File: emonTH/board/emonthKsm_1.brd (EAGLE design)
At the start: 50 x 50 mm, 9 parts

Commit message: Added board
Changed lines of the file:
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@@
 </variantdefs>
 <classes>
-<class number="0" name="default" width="0" drill="0">
+<class number="0" name="default" width="0.3" drill="0.5">
+<clearance class="0" value="0.3"/>
 </class>
 </classes>
-<designrules name="default">
+<designrules name="SeeedStudio_2layer_DRU_no_angle_20140221">
 <description language="de">&lt;b&gt;EAGLE Design Rules&lt;/b&gt;
 &lt;p&gt;
@@
 necessary adjustments and save your customized
 design rules under a new name.</description>
+<description language="zh">&lt;b&gt;Seeed Studio EAGLE Design Rules&lt;/b&gt;
+</description>
 <param name="layerSetup" value="(1*16)"/>
-<param name="mtCopper" value="0.035mm 0.035mm 0.035mm 0.035mm 0.035mm 0.035mm 0.035mm 0.035mm 0.035mm 0.035mm 0.035mm 0.035mm 0.035mm 0.035mm 0.035mm 0.035mm"/>
-<param name="mtIsolate" value="1.5mm 0.15mm 0.2mm 0.15mm 0.2mm 0.15mm 0.2mm 0.15mm 0.2mm 0.15mm 0.2mm 0.15mm 0.2mm 0.15mm 0.2mm"/>
-<param name="mdWireWire" value="8mil"/>
-<param name="mdWirePad" value="8mil"/>
-<param name="mdWireVia" value="8mil"/>
-<param name="mdPadPad" value="8mil"/>
-<param name="mdPadVia" value="8mil"/>
-<param name="mdViaVia" value="8mil"/>
-<param name="mdSmdPad" value="8mil"/>
-<param name="mdSmdVia" value="8mil"/>
-<param name="mdSmdSmd" value="8mil"/>
+<param name="mtCopper" value="0.035mm 0.0175mm 0.035mm 0.035mm 0.035mm 0.035mm 0.035mm 0.035mm 0.035mm 0.035mm 0.035mm 0.035mm 0.035mm 0.035mm 0.0175mm 0.035mm"/>
+<param name="mtIsolate" value="1.5mm 1.1mm 0.2mm 0.15mm 0.2mm 0.15mm 0.2mm 0.15mm 0.2mm 0.15mm 0.2mm 0.15mm 0.2mm 0.15mm 0.2mm"/>
+<param name="mdWireWire" value="6mil"/>
+<param name="mdWirePad" value="6mil"/>
+<param name="mdWireVia" value="6mil"/>
+<param name="mdPadPad" value="6mil"/>
+<param name="mdPadVia" value="6mil"/>
+<param name="mdViaVia" value="6mil"/>
+<param name="mdSmdPad" value="0mil"/>
+<param name="mdSmdVia" value="0mil"/>
+<param name="mdSmdSmd" value="0mil"/>
 <param name="mdViaViaSameLayer" value="8mil"/>
 <param name="mnLayersViaInSmd" value="2"/>
-<param name="mdCopperDimension" value="40mil"/>
-<param name="mdDrill" value="8mil"/>
+<param name="mdCopperDimension" value="10mil"/>
+<param name="mdDrill" value="10mil"/>
 <param name="mdSmdStop" value="0mil"/>
-<param name="msWidth" value="10mil"/>
-<param name="msDrill" value="24mil"/>
-<param name="msMicroVia" value="9.99mm"/>
+<param name="msWidth" value="6mil"/>
+<param name="msDrill" value="12mil"/>
+<param name="msMicroVia" value="12mil"/>
 <param name="msBlindViaRatio" value="0.5"/>
 <param name="rvPadTop" value="0.25"/>
@@
 <param name="rlMinPadBottom" value="10mil"/>
 <param name="rlMaxPadBottom" value="20mil"/>
-<param name="rlMinViaOuter" value="8mil"/>
+<param name="rlMinViaOuter" value="6mil"/>
 <param name="rlMaxViaOuter" value="20mil"/>
-<param name="rlMinViaInner" value="8mil"/>
+<param name="rlMinViaInner" value="6mil"/>
 <param name="rlMaxViaInner" value="20mil"/>
 <param name="rlMinMicroViaOuter" value="4mil"/>
@@
 <param name="psTop" value="-1"/>
 <param name="psBottom" value="-1"/>
-<param name="psFirst" value="-1"/>
+<param name="psFirst" value="0"/>
 <param name="psElongationLong" value="100"/>
 <param name="psElongationOffset" value="100"/>
 <param name="mvStopFrame" value="1"/>
 <param name="mvCreamFrame" value="0"/>
-<param name="mlMinStopFrame" value="4mil"/>
-<param name="mlMaxStopFrame" value="4mil"/>
+<param name="mlMinStopFrame" value="2mil"/>
+<param name="mlMaxStopFrame" value="2mil"/>
 <param name="mlMinCreamFrame" value="0mil"/>
 <param name="mlMaxCreamFrame" value="0mil"/>
-<param name="mlViaStopLimit" value="0mil"/>
+<param name="mlViaStopLimit" value="100mil"/>
 <param name="srRoundness" value="0"/>
 <param name="srMinRoundness" value="0mil"/>
@@
 <param name="checkAngle" value="0"/>
 <param name="checkFont" value="1"/>
-<param name="checkRestrict" value="1"/>
+<param name="checkRestrict" value="0"/>
 <param name="useDiameter" value="13"/>
 <param name="maxErrors" value="50"/>
@@
 <param name="RoutingGrid" value="50mil"/>
 <param name="AutoGrid" value="1"/>
-<param name="Efforts" value="0"/>
+<param name="Efforts" value="2"/>
 <param name="TopRouterVariant" value="1"/>
 <param name="tpViaShape" value="round"/>
@@
 <param name="PrefDir.14" value="0"/>
 <param name="PrefDir.15" value="0"/>
-<param name="PrefDir.16" value="a"/>
+<param name="PrefDir.16" value="0"/>
 <param name="cfVia" value="8"/>
 <param name="cfNonPref" value="5"/>
@@
 <element name="ARDUINO" library="Arduino-clone" package="ABK-PRO-MINI" value="ABK-PRO-MINI" x="11.91" y="33.91"/>
 <element name="RFM69" library="Eagle-JeeLabs" package="RFM12B/69CW" value="RFM12B/69CW" x="36.45" y="11.89"/>
-<element name="DS18B20" library="Eagle-JeeLabs" package="TO-92" value="TEMPERATURE-SENSOR" x="33.1" y="44.19"/>
+<element name="DS18B20" library="Eagle-JeeLabs" package="TO-92" value="TEMPERATURE-SENSOR" x="33.1" y="44.19" smashed="yes">
+<attribute name="NAME" x="36.275" y="44.825" size="0.4064" layer="25" ratio="10"/>
+</element>
 <element name="ANT1" library="discrete" package="PAD-01" value="" x="46.67" y="2.52"/>
 <element name="AMS2302" library="RHT03_DHT-22_AM2302" package="RHT03_DHT-22" value="" x="35.94" y="30.55">
@@
 <contactref element="C1" pad="2"/>
 <contactref element="DS18B20" pad="1"/>
+<wire x1="39.75" y1="30.55" x2="47.44" y2="35.93" width="0" layer="19" extent="1-1"/>
+<wire x1="31.83" y1="44.19" x2="39.75" y2="30.55" width="0" layer="19" extent="1-1"/>
+<wire x1="22.07" y1="37.72" x2="31.83" y2="44.19" width="0" layer="19" extent="1-1"/>
 <wire x1="6.83" y1="32.64" x2="22.07" y2="37.72" width="0" layer="19" extent="1-1"/>
 <wire x1="13.18" y1="12.32" x2="6.83" y2="32.64" width="0" layer="19" extent="1-1"/>
-<wire x1="45.5096" y1="9.89" x2="13.18" y2="12.32" width="0" layer="19" extent="1-1"/>
-<wire x1="28.95" y1="5.89" x2="45.5096" y2="9.89" width="0" layer="19" extent="1-1"/>
-<wire x1="31.83" y1="44.19" x2="28.95" y2="5.89" width="0" layer="19" extent="1-1"/>
-<wire x1="39.75" y1="30.55" x2="31.83" y2="44.19" width="0" layer="19" extent="1-1"/>
-<wire x1="47.44" y1="35.93" x2="39.75" y2="30.55" width="0" layer="19" extent="1-1"/>
+<wire x1="28.95" y1="5.89" x2="13.18" y2="12.32" width="0" layer="19" extent="1-1"/>
+<wire x1="45.5096" y1="9.89" x2="28.95" y2="5.89" width="0" layer="19" extent="1-1"/>
 </signal>
 <signal name="A0">
@@
 <contactref element="DS18B20" pad="2"/>
 <contactref element="R5" pad="2"/>
-<wire x1="33.1" y1="46.095" x2="22.07" y2="30.1" width="0" layer="19" extent="1-1"/>
-<wire x1="43.44" y1="47.31" x2="33.1" y2="46.095" width="0" layer="19" extent="1-1"/>
+<wire x1="33.1" y1="46.095" x2="43.44" y2="47.31" width="0" layer="19" extent="1-1"/>
+<wire x1="22.07" y1="30.1" x2="33.1" y2="46.095" width="0" layer="19" extent="1-1"/>
 </signal>
 <signal name="A1">
@@
 <contactref element="AMS2302" pad="DATA"/>
 <contactref element="R4" pad="2"/>
-<wire x1="34.67" y1="30.55" x2="22.07" y2="27.56" width="0" layer="19" extent="1-1"/>
-<wire x1="39.44" y1="35.12" x2="34.67" y2="30.55" width="0" layer="19" extent="1-1"/>
+<wire x1="34.67" y1="30.55" x2="39.44" y2="35.12" width="0" layer="19" extent="1-1"/>
+<wire x1="22.07" y1="27.56" x2="34.67" y2="30.55" width="0" layer="19" extent="1-1"/>
 </signal>
 <signal name="D10">
@@
 <contactref element="RFM69" pad="SEL"/>
 <contactref element="R1" pad="1"/>
-<wire x1="44.95" y1="17.89" x2="22.07" y2="12.32" width="0" layer="19" extent="1-1"/>
-<wire x1="45.74" y1="22.5" x2="44.95" y2="17.89" width="0" layer="19" extent="1-1"/>
+<wire x1="44.95" y1="17.89" x2="45.74" y2="22.5" width="0" layer="19" extent="1-1"/>
+<wire x1="22.07" y1="12.32" x2="44.95" y2="17.89" width="0" layer="19" extent="1-1"/>
 </signal>
 <signal name="D11">
 <contactref element="ARDUINO" pad="D11"/>
 <contactref element="RFM69" pad="SDI"/>
-<wire x1="44.95" y1="13.89" x2="22.07" y2="14.86" width="0" layer="19" extent="1-1"/>
+<wire x1="22.07" y1="14.86" x2="44.95" y2="13.89" width="0" layer="19" extent="1-1"/>
 </signal>
 <signal name="D12">
 <contactref element="ARDUINO" pad="D12"/>
 <contactref element="RFM69" pad="SDO"/>
-<wire x1="28.95" y1="17.89" x2="22.07" y2="17.4" width="0" layer="19" extent="1-1"/>
+<wire x1="22.07" y1="17.4" x2="28.95" y2="17.89" width="0" layer="19" extent="1-1"/>
 </signal>
 <signal name="D13">
 <contactref element="ARDUINO" pad="D13"/>
 <contactref element="RFM69" pad="SCK"/>
-<wire x1="44.95" y1="15.89" x2="22.07" y2="19.94" width="0" layer="19" extent="1-1"/>
+<wire x1="22.07" y1="19.94" x2="44.95" y2="15.89" width="0" layer="19" extent="1-1"/>
 </signal>
 <signal name="VIN">
@@
 <contactref element="ARDUINO" pad="VCC"/>
 <contactref element="R1" pad="2"/>
-<wire x1="44.95" y1="7.89" x2="22.07" y2="32.64" width="0" layer="19" extent="1-1"/>
-<wire x1="47.44" y1="22.5" x2="44.95" y2="7.89" width="0" layer="19" extent="1-1"/>
+<wire x1="44.95" y1="7.89" x2="47.44" y2="22.5" width="0" layer="19" extent="1-1"/>
+<wire x1="22.07" y1="32.64" x2="47.44" y2="22.5" width="0" layer="19" extent="1-1"/>
 </signal>
 <signal name="D5">
@@
 <contactref element="R5" pad="1"/>
 <contactref element="ARDUINO" pad="D5"/>
-<wire x1="34.37" y1="44.19" x2="6.83" y2="22.48" width="0" layer="19" extent="1-1"/>
-<wire x1="41.74" y1="47.31" x2="34.37" y2="44.19" width="0" layer="19" extent="1-1"/>
+<wire x1="34.37" y1="44.19" x2="41.74" y2="47.31" width="0" layer="19" extent="1-1"/>
+<wire x1="6.83" y1="22.48" x2="34.37" y2="44.19" width="0" layer="19" extent="1-1"/>
 </signal>
 <signal name="D6">
@@
 <contactref element="R4" pad="1"/>
 <contactref element="ARDUINO" pad="D6"/>
-<wire x1="32.13" y1="30.55" x2="6.83" y2="19.94" width="0" layer="19" extent="1-1"/>
-<wire x1="37.74" y1="35.12" x2="32.13" y2="30.55" width="0" layer="19" extent="1-1"/>
+<wire x1="32.13" y1="30.55" x2="37.74" y2="35.12" width="0" layer="19" extent="1-1"/>
+<wire x1="6.83" y1="19.94" x2="32.13" y2="30.55" width="0" layer="19" extent="1-1"/>
 </signal>
 </signals>
+<errors>
+</errors>
 </board>
 </drawing>

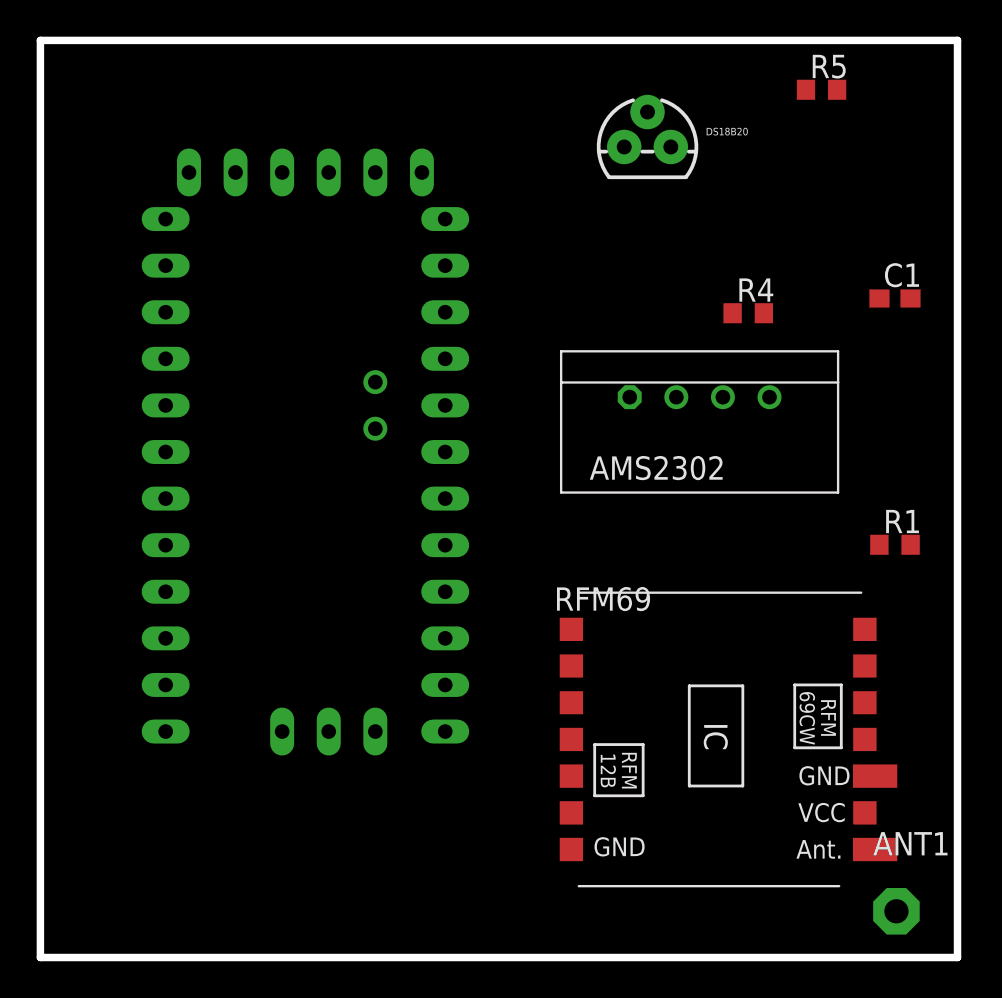
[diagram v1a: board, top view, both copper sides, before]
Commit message: Replaced smd components with regular
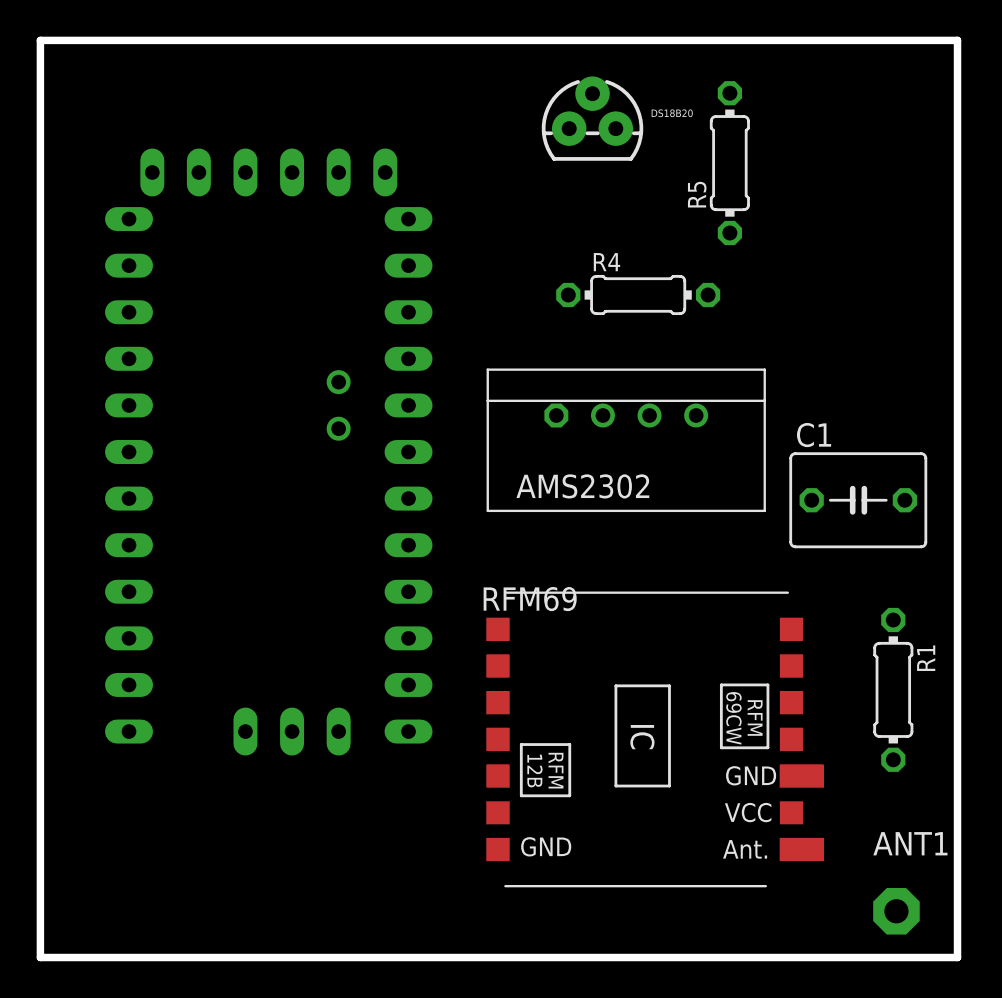
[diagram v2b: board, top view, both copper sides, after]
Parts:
- C1: device resistor:C0603 -> rcl:C050-050X075
- R1, R5: device resistor:R0603 -> rcl:0204/7
- R4: value (none) -> 10k; device resistor:R0603 -> rcl:0204/7
- moved C1 11.2 mm to (44.6, 24.9)
- moved R1 7.91 mm to (46.5, 14.6), turned to 270 degrees
- moved R5 6.40 mm to (37.6, 43.3), turned to 90 degrees
- moved R4 6.08 mm to (32.6, 36.1)
- moved AMS2302 4.12 mm to (31.9, 29.6)
- moved RFM69 4.00 mm to (32.5, 11.9)
- moved DS18B20 3.16 mm to (30.1, 45.2)
- moved ARDUINO 2.00 mm to (9.91, 33.9)
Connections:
- net 3.3V: now also C1.1
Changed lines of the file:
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@@
 </autorouter>
 <elements>
-<element name="ARDUINO" library="Arduino-clone" package="ABK-PRO-MINI" value="ABK-PRO-MINI" x="11.91" y="33.91"/>
-<element name="RFM69" library="Eagle-JeeLabs" package="RFM12B/69CW" value="RFM12B/69CW" x="36.45" y="11.89"/>
-<element name="DS18B20" library="Eagle-JeeLabs" package="TO-92" value="TEMPERATURE-SENSOR" x="33.1" y="44.19" smashed="yes">
-<attribute name="NAME" x="36.275" y="44.825" size="0.4064" layer="25" ratio="10"/>
+<element name="ARDUINO" library="Arduino-clone" package="ABK-PRO-MINI" value="ABK-PRO-MINI" x="9.91" y="33.91"/>
+<element name="RFM69" library="Eagle-JeeLabs" package="RFM12B/69CW" value="RFM12B/69CW" x="32.45" y="11.89"/>
+<element name="DS18B20" library="Eagle-JeeLabs" package="TO-92" value="TEMPERATURE-SENSOR" x="30.1" y="45.19" smashed="yes">
+<attribute name="NAME" x="33.275" y="45.825" size="0.4064" layer="25" ratio="10"/>
 </element>
 <element name="ANT1" library="discrete" package="PAD-01" value="" x="46.67" y="2.52"/>
-<element name="AMS2302" library="RHT03_DHT-22_AM2302" package="RHT03_DHT-22" value="" x="35.94" y="30.55">
-<attribute name="PROD_ID" value="SEN-10167" x="35.94" y="30.55" size="1.778" layer="27" display="off"/>
+<element name="AMS2302" library="RHT03_DHT-22_AM2302" package="RHT03_DHT-22" value="" x="31.94" y="29.55">
+<attribute name="PROD_ID" value="SEN-10167" x="31.94" y="29.55" size="1.778" layer="27" display="off"/>
 </element>
-<element name="C1" library="resistor" package="C0603" value="100nf" x="46.59" y="35.93"/>
-<element name="R4" library="resistor" package="R0603" value="" x="38.59" y="35.12"/>
-<element name="R5" library="resistor" package="R0603" value="4.7k" x="42.59" y="47.31"/>
-<element name="R1" library="resistor" package="R0603" value="100k" x="46.59" y="22.5"/>
+<element name="C1" library="rcl" package="C050-050X075" value="100nf" x="44.59" y="24.93"/>
+<element name="R4" library="rcl" package="0204/7" value="10k" x="32.59" y="36.12"/>
+<element name="R5" library="rcl" package="0204/7" value="4.7k" x="37.59" y="43.31" rot="R90"/>
+<element name="R1" library="rcl" package="0204/7" value="100k" x="46.5" y="14.59" rot="R270"/>
 </elements>
 <signals>
@@
 <contactref element="ARDUINO" pad="GND"/>
 <contactref element="AMS2302" pad="GND"/>
+<contactref element="DS18B20" pad="1"/>
 <contactref element="C1" pad="2"/>
-<contactref element="DS18B20" pad="1"/>
-<wire x1="39.75" y1="30.55" x2="47.44" y2="35.93" width="0" layer="19" extent="1-1"/>
-<wire x1="31.83" y1="44.19" x2="39.75" y2="30.55" width="0" layer="19" extent="1-1"/>
-<wire x1="22.07" y1="37.72" x2="31.83" y2="44.19" width="0" layer="19" extent="1-1"/>
-<wire x1="6.83" y1="32.64" x2="22.07" y2="37.72" width="0" layer="19" extent="1-1"/>
-<wire x1="13.18" y1="12.32" x2="6.83" y2="32.64" width="0" layer="19" extent="1-1"/>
-<wire x1="28.95" y1="5.89" x2="13.18" y2="12.32" width="0" layer="19" extent="1-1"/>
-<wire x1="45.5096" y1="9.89" x2="28.95" y2="5.89" width="0" layer="19" extent="1-1"/>
+<wire x1="20.07" y1="37.72" x2="28.83" y2="45.19" width="0" layer="19" extent="1-1"/>
+<wire x1="4.83" y1="32.64" x2="20.07" y2="37.72" width="0" layer="19" extent="1-1"/>
+<wire x1="35.75" y1="29.55" x2="28.83" y2="45.19" width="0" layer="19" extent="1-1"/>
+<wire x1="47.13" y1="24.93" x2="35.75" y2="29.55" width="0" layer="19" extent="1-1"/>
+<wire x1="41.5096" y1="9.89" x2="47.13" y2="24.93" width="0" layer="19" extent="1-1"/>
+<wire x1="24.95" y1="5.89" x2="41.5096" y2="9.89" width="0" layer="19" extent="1-1"/>
+<wire x1="11.18" y1="12.32" x2="24.95" y2="5.89" width="0" layer="19" extent="1-1"/>
 </signal>
 <signal name="A0">
@@
 <contactref element="DS18B20" pad="2"/>
 <contactref element="R5" pad="2"/>
-<wire x1="33.1" y1="46.095" x2="43.44" y2="47.31" width="0" layer="19" extent="1-1"/>
-<wire x1="22.07" y1="30.1" x2="33.1" y2="46.095" width="0" layer="19" extent="1-1"/>
+<wire x1="30.1" y1="47.095" x2="37.59" y2="47.12" width="0" layer="19" extent="1-1"/>
+<wire x1="20.07" y1="30.1" x2="30.1" y2="47.095" width="0" layer="19" extent="1-1"/>
 </signal>
 <signal name="A1">
@@
 <contactref element="AMS2302" pad="DATA"/>
 <contactref element="R4" pad="2"/>
-<wire x1="34.67" y1="30.55" x2="39.44" y2="35.12" width="0" layer="19" extent="1-1"/>
-<wire x1="22.07" y1="27.56" x2="34.67" y2="30.55" width="0" layer="19" extent="1-1"/>
+<wire x1="30.67" y1="29.55" x2="36.4" y2="36.12" width="0" layer="19" extent="1-1"/>
+<wire x1="20.07" y1="27.56" x2="30.67" y2="29.55" width="0" layer="19" extent="1-1"/>
 </signal>
 <signal name="D10">
@@
 <contactref element="RFM69" pad="SEL"/>
 <contactref element="R1" pad="1"/>
-<wire x1="44.95" y1="17.89" x2="45.74" y2="22.5" width="0" layer="19" extent="1-1"/>
-<wire x1="22.07" y1="12.32" x2="44.95" y2="17.89" width="0" layer="19" extent="1-1"/>
+<wire x1="40.95" y1="17.89" x2="46.5" y2="18.4" width="0" layer="19" extent="1-1"/>
+<wire x1="20.07" y1="12.32" x2="40.95" y2="17.89" width="0" layer="19" extent="1-1"/>
 </signal>
 <signal name="D11">
 <contactref element="ARDUINO" pad="D11"/>
 <contactref element="RFM69" pad="SDI"/>
-<wire x1="22.07" y1="14.86" x2="44.95" y2="13.89" width="0" layer="19" extent="1-1"/>
+<wire x1="20.07" y1="14.86" x2="40.95" y2="13.89" width="0" layer="19" extent="1-1"/>
 </signal>
 <signal name="D12">
 <contactref element="ARDUINO" pad="D12"/>
 <contactref element="RFM69" pad="SDO"/>
-<wire x1="22.07" y1="17.4" x2="28.95" y2="17.89" width="0" layer="19" extent="1-1"/>
+<wire x1="20.07" y1="17.4" x2="24.95" y2="17.89" width="0" layer="19" extent="1-1"/>
 </signal>
 <signal name="D13">
 <contactref element="ARDUINO" pad="D13"/>
 <contactref element="RFM69" pad="SCK"/>
-<wire x1="22.07" y1="19.94" x2="44.95" y2="15.89" width="0" layer="19" extent="1-1"/>
+<wire x1="20.07" y1="19.94" x2="40.95" y2="15.89" width="0" layer="19" extent="1-1"/>
 </signal>
 <signal name="VIN">
@@
 <contactref element="RFM69" pad="ANT"/>
 <contactref element="ANT1" pad="1"/>
-<wire x1="46.67" y1="2.52" x2="45.5096" y2="5.89" width="0" layer="19" extent="1-1"/>
+<wire x1="46.67" y1="2.52" x2="41.5096" y2="5.89" width="0" layer="19" extent="1-1"/>
 </signal>
 <signal name="D2">
@@
 <contactref element="ARDUINO" pad="VCC"/>
 <contactref element="R1" pad="2"/>
-<wire x1="44.95" y1="7.89" x2="47.44" y2="22.5" width="0" layer="19" extent="1-1"/>
-<wire x1="22.07" y1="32.64" x2="47.44" y2="22.5" width="0" layer="19" extent="1-1"/>
+<contactref element="C1" pad="1"/>
+<wire x1="46.5" y1="10.78" x2="42.05" y2="24.93" width="0" layer="19" extent="1-1"/>
+<wire x1="40.95" y1="7.89" x2="46.5" y2="10.78" width="0" layer="19" extent="1-1"/>
+<wire x1="20.07" y1="32.64" x2="42.05" y2="24.93" width="0" layer="19" extent="1-1"/>
 </signal>
 <signal name="D5">
@@
 <contactref element="R5" pad="1"/>
 <contactref element="ARDUINO" pad="D5"/>
-<wire x1="34.37" y1="44.19" x2="41.74" y2="47.31" width="0" layer="19" extent="1-1"/>
-<wire x1="6.83" y1="22.48" x2="34.37" y2="44.19" width="0" layer="19" extent="1-1"/>
+<wire x1="31.37" y1="45.19" x2="37.59" y2="39.5" width="0" layer="19" extent="1-1"/>
+<wire x1="4.83" y1="22.48" x2="31.37" y2="45.19" width="0" layer="19" extent="1-1"/>
 </signal>
 <signal name="D6">
@@
 <contactref element="R4" pad="1"/>
 <contactref element="ARDUINO" pad="D6"/>
-<wire x1="32.13" y1="30.55" x2="37.74" y2="35.12" width="0" layer="19" extent="1-1"/>
-<wire x1="6.83" y1="19.94" x2="32.13" y2="30.55" width="0" layer="19" extent="1-1"/>
+<wire x1="28.13" y1="29.55" x2="28.78" y2="36.12" width="0" layer="19" extent="1-1"/>
+<wire x1="4.83" y1="19.94" x2="28.13" y2="29.55" width="0" layer="19" extent="1-1"/>
 </signal>
 </signals>

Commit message: Update emonthKSM board
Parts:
- added FRAME1: FRAME-LETTERNO_PACKAGE, SparkFun-Aesthetics:DUMMY
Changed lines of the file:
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@@
 <element name="R5" library="rcl" package="0204/7" value="4.7k" x="37.59" y="43.31" rot="R90"/>
 <element name="R1" library="rcl" package="0204/7" value="100k" x="46.5" y="14.59" rot="R270"/>
+<element name="FRAME1" library="SparkFun-Aesthetics" package="DUMMY" value="FRAME-LETTERNO_PACKAGE" x="0" y="-1">
+<attribute name="VERSION" value="v01" x="0" y="-1" size="1.778" layer="27" display="off"/>
+<attribute name="DESIGNER" value="Nobody" x="0" y="-1" size="1.778" layer="27" display="off"/>
+</element>
 </elements>
 <signals>
